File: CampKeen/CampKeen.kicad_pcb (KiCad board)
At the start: 4 copper layers, 177.8 x 142.2 mm, 181 parts, among them IC1 LM2597MX-ADJ_NOPB, IC2 LM2670SX-5.0_NOPB, IC3 DS3231SN#, IC4 CD74HC4050ME4, IC5 TL071CP, J1 Vin, J2 CircuitSetupsSplitPhase, J3 Vin, J4 Screw_Terminal_01x04, J5 GenEnclosure, J6 GenHeadL, J7 GenHeadR, K1 DIP05-1A72-12L, K2 DIP05-1A72-12L, K4 DIP05-1A72-12L, P1 Power, P10 CONN_01X01, P11 CONN_01X01, P12 CONN_01X01, P13 CONN_01X01, P2 Analog, P3 Analog, P4 Digital, P5 PWM, P6 PWM, P7 Communication, P8 CONN_01X01, P9 CONN_01X01, Q1 BC547, Q10 2N7000, Q11 2N7000, Q12 2N7000, Q13 2N7000, Q14 2N7000, Q15 IRF510, Q16 2N7000, Q17 IRF510, Q18 2N7000, Q19 IRF510, Q2 2N7000, Q20 2N7000, Q21 IRF510, Q22 BC547, Q23 2N7000, Q24 IRF510, Q25 2N7000, Q26 2N7000, Q27 IRF510, Q28 2N7000, Q29 IRF510, Q3 2N7000, Q30 2N7000, Q31 IRF510, Q32 BC547, Q33 2N7000, Q35 2N7000, Q36 IRF510, Q37 2N7000, Q38 IRF510, Q39 IRF510, Q4 2N7000, Q40 IRF9Z34NPBF, Q5 2N7000, Q6 BC547, Q7 2N7000, Q8 2N7000, Q9 2N7000, U2 MAX232

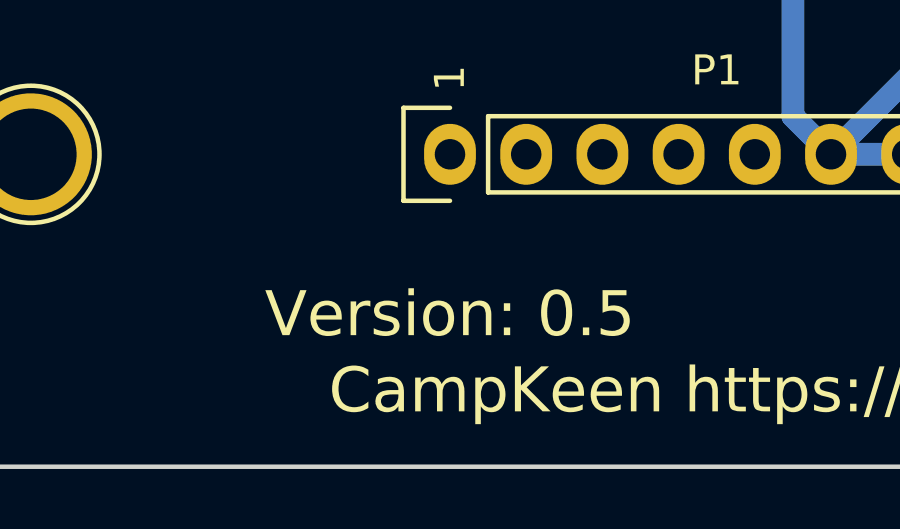
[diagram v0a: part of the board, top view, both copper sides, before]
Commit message: forgot to bump the version number to 0.6 on the PCB Silkscreen
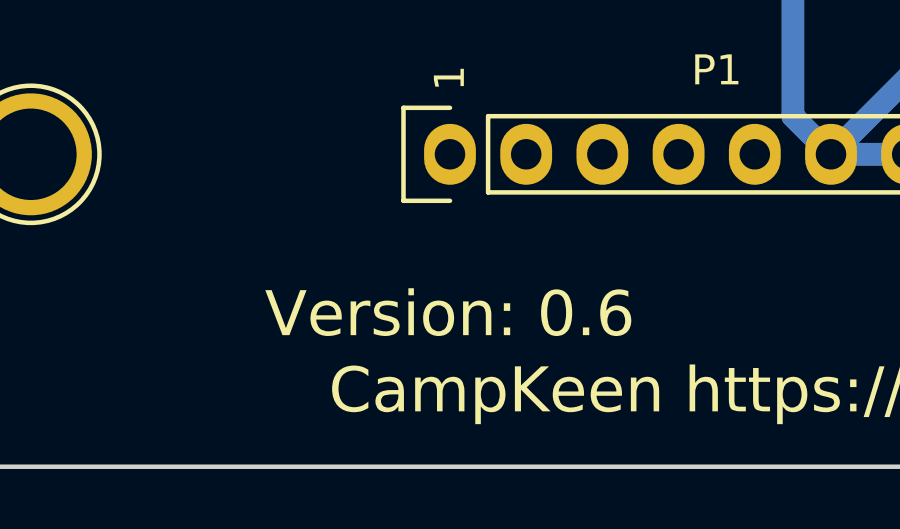
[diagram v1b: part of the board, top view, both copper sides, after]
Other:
- board text added: "Version: 0.6"
- board text removed: "Version: 0.5"

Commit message: adding docs and cleaning up pin mappings and extra parts for ports.
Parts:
- removed Q35: 2N7000, Package_TO_SOT_THT:TO-92_Inline
- removed R81, R83: 1M, Resistor_THT:R_Axial_DIN0207_L6.3mm_D2.5mm_P2.54mm_Vertical
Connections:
- IO1 pad 10: Net-(IO1-Pad10) -> (no net)
- Temps1 pad 4: +5V -> (no net)
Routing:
- net Net-(IO1-Pad10): track 131.6 -> 0.00 mm, vias 1 -> 0
- net Net-(Q35-Pad1): track 7.17 -> 0.00 mm
- net +5V: track 708.0 -> 701.8 mm

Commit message: continue on fixing and adding stuff. fixed the fuck up on the schematic for the 5to3 volt converter. changing out the voltage sensor to a opa2340, ading asecond general voltage sensor. and an additional NTC sensor. RTC Battery monitor.
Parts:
- added J8: Conn_01x02, Connector_PinHeader_2.54mm:PinHeader_1x02_P2.54mm_Vertical, F.Cu at (95.8, 6.35)
- added R25: 10k, Resistor_THT:R_Axial_DIN0207_L6.3mm_D2.5mm_P2.54mm_Vertical, F.Cu at (127.5, 165.1)
- added R29: 47K, Resistor_THT:R_Axial_DIN0207_L6.3mm_D2.5mm_P2.54mm_Vertical, F.Cu at (95.8, -6.35)
- added RV1: R_POT_US, Potentiometer_THT:Potentiometer_Bourns_3296W_Vertical, F.Cu at (90.4, 7.25)
- IC5: value TL071CP -> OPA2340PA
- moved IC5 28.0 mm to (88.1, -2.54)
- renumbered Tanks2 to Tanks0
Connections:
- net /A10 renamed A10
- net /A3 renamed A3
- net /A4 renamed A4
- net /A5 renamed A5
- net /A6 renamed A6
- net /A7 renamed A7
- net /A8 renamed A8
- net /A9 renamed A9
- net /CS renamed /3.3CS
- net /SCLK renamed /3.3SCLK
- IC3 pad 14: Net-(IC3-Pad14) -> A14
- IC4 pad 5: /50(MISO) -> /3.3MISO
- IC4 pad 6: /51(MOSI) -> /3.3MOSI
- IC5 pad 1: (no net) -> A0
- IC5 pad 2: /A0 -> A0
- IC5 pad 5: (no net) -> Net-(IC5-Pad5)
- IC5 pad 6: /A0 -> A12
- IC5 pad 7: +5V -> A12
- IC5 pad 8: (no net) -> +5V
- IO1 pad 10: (no net) -> AUXVoltage
- J2 pad 3: /51(MOSI) -> /3.3MOSI
- J2 pad 4: /50(MISO) -> /3.3MISO
- P2 pad 1: /A0 -> A0
- P3 pad 4: (no net) -> A11
- P3 pad 5: (no net) -> A12
- P3 pad 7: /A14 -> A14
- P3 pad 8: /A15 -> (no net)
- R35 pad 2: /A0 -> A0
- RTCBattery1 pad 1: Net-(IC3-Pad14) -> A14
- Tanks0 pad 11: /A14 -> (no net)
- Tanks0 pad 12: /A15 -> (no net)
- Temps1 pad 4: (no net) -> A11
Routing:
- net /50(MISO): track 251.5 -> 0.00 mm, vias 1 -> 0
- net /51(MOSI): track 251.4 -> 0.00 mm, vias 1 -> 0
- net /A0: track 150.9 -> 0.00 mm
- net /A15: track 137.5 -> 0.00 mm, vias 4 -> 0
- net /A14: track 131.4 -> 0.00 mm
- net Net-(IC3-Pad14): track 36.4 -> 0.00 mm, vias 2 -> 0
- net A14: track 0.00 -> 36.4 mm, vias 0 -> 2
- net GND: track 892.0 -> 875.8 mm
- net Net-(IC5-Pad3): track 20.3 -> 6.13 mm
- net +5V: track 701.8 -> 693.3 mm

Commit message: updated the pin mapping to the terms. cleaned up the Schematic. PCB placement and routing is what is left to do.
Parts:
- removed the IC5 at (88.1, -2.54)
- removed the J4 at (52.6, 95.2)
- removed K1, K2, K4: DIP05-1A72-12L, SamacSys_Parts:DIP051A7212L
- removed the Q1 at (182.1, 127.0)
- removed the R10 at (164.3, 128.8)
- removed the R7 at (182.6, 121.9)
- removed the R8 at (182.6, 116.8)
- removed the R9 at (159.3, 128.8)
- added 5VOut1: VS, SamacSys_Parts:BK_HTC-15M, F.Cu at (-49.0, -77.5)
- added C16: 22nF, Capacitor_THT:C_Disc_D4.7mm_W2.5mm_P5.00mm, F.Cu at (58.5, -26.7)
- added C17: 22nF, Capacitor_THT:C_Disc_D4.7mm_W2.5mm_P5.00mm, F.Cu at (71.9, -34.2)
- added C18: 22nF, Capacitor_THT:C_Disc_D4.7mm_W2.5mm_P5.00mm, F.Cu at (86.3, -38.1)
- added C19: 22nF, Capacitor_THT:C_Disc_D4.7mm_W2.5mm_P5.00mm, F.Cu at (58.5, -30.7)
- added C20: 22nF, Capacitor_THT:C_Disc_D4.7mm_W2.5mm_P5.00mm, F.Cu at (-97.3, -70.3)
- added C21: 22nF, Capacitor_THT:C_Disc_D4.7mm_W2.5mm_P5.00mm, F.Cu at (-110.7, -66.9)
- added C22: 22nF, Capacitor_THT:C_Disc_D4.7mm_W2.5mm_P5.00mm, F.Cu at (-82.9, -74.3)
- added C23: 22nF, Capacitor_THT:C_Disc_D4.7mm_W2.5mm_P5.00mm, F.Cu at (-110.7, -62.8)
- added C24: 22nF, Capacitor_THT:C_Disc_D4.7mm_W2.5mm_P5.00mm, F.Cu at (4.61, -12.7)
- added C25: 22nF, Capacitor_THT:C_Disc_D4.7mm_W2.5mm_P5.00mm, F.Cu at (4.61, -8.70)
- added C26: 22nF, Capacitor_THT:C_Disc_D4.7mm_W2.5mm_P5.00mm, F.Cu at (12.8, -12.7)
- added C27: 22nF, Capacitor_THT:C_Disc_D4.7mm_W2.5mm_P5.00mm, F.Cu at (4.61, -4.64)
- added C28: 22nF, Capacitor_THT:C_Disc_D4.7mm_W2.5mm_P5.00mm, F.Cu at (12.8, -36.3)
- added C29: 22nF, Capacitor_THT:C_Disc_D4.7mm_W2.5mm_P5.00mm, F.Cu at (20.9, -44.4)
- added C30: 22nF, Capacitor_THT:C_Disc_D4.7mm_W2.5mm_P5.00mm, F.Cu at (4.61, -32.2)
- added C31: 22nF, Capacitor_THT:C_Disc_D4.7mm_W2.5mm_P5.00mm, F.Cu at (12.8, -40.3)
- added C32: 22nF, Capacitor_THT:C_Disc_D4.7mm_W2.5mm_P5.00mm, F.Cu at (4.61, -36.3)
- added C33: 22nF, Capacitor_THT:C_Disc_D4.7mm_W2.5mm_P5.00mm, F.Cu at (12.8, -44.4)
- added C34: 22nF, Capacitor_THT:C_Disc_D4.7mm_W2.5mm_P5.00mm, F.Cu at (4.61, -40.3)
- added C35: 22nF, Capacitor_THT:C_Disc_D4.7mm_W2.5mm_P5.00mm, F.Cu at (4.61, -44.4)
- added C36: 22nF, Capacitor_THT:C_Disc_D4.7mm_W2.5mm_P5.00mm, F.Cu at (20.9, -40.3)
- added C37: 22nF, Capacitor_THT:C_Disc_D4.7mm_W2.5mm_P5.00mm, F.Cu at (4.61, -28.2)
- added IC4: OPA2340PA, SamacSys_Parts:DIP794W53P254L959H508Q8N, F.Cu at (-29.7, -76.7)
- added IC6: OPA2340PA, SamacSys_Parts:DIP794W53P254L959H508Q8N, F.Cu at (-57.5, -66.5)
- added J3: Conn_01x02, Connector_PinHeader_2.54mm:PinHeader_1x02_P2.54mm_Vertical, F.Cu at (-21.9, -73.0)
- added J9: Conn_01x02, Connector_PinHeader_2.54mm:PinHeader_1x02_P2.54mm_Vertical, F.Cu at (-21.9, -80.2)
- added Q34: IRF9Z34NPBF, SamacSys_Parts:TO254P469X1042X1967-3P, F.Cu at (32.0, -71.4)
- added Q35: 2N7000, Package_TO_SOT_THT:TO-92_Inline, F.Cu at (30.5, -65.9)
- added Q40: 2N7000, Package_TO_SOT_THT:TO-92_Inline, F.Cu at (50.4, -75.6)
- added Q41: IRF9Z34NPBF, SamacSys_Parts:TO254P469X1042X1967-3P, F.Cu at (6.54, -57.5)
- added Q42: IRF9Z34NPBF, SamacSys_Parts:TO254P469X1042X1967-3P, F.Cu at (33.3, -77.7)
- added Q43: 2N7000, Package_TO_SOT_THT:TO-92_Inline, F.Cu at (43.9, -75.6)
- added Q44: IRF9Z34NPBF, SamacSys_Parts:TO254P469X1042X1967-3P, F.Cu at (46.7, -81.1)
- added Q45: 2N7000, Package_TO_SOT_THT:TO-92_Inline, F.Cu at (5.02, -52.0)
- added Q46: IRF9Z34NPBF, SamacSys_Parts:TO254P469X1042X1967-3P, F.Cu at (19.9, -68.0)
- added Q47: 2N7000, Package_TO_SOT_THT:TO-92_Inline, F.Cu at (126.9, -11.9)
- added Q48: IRF9Z34NPBF, SamacSys_Parts:TO254P469X1042X1967-3P, F.Cu at (136.6, -20.9)
- added Q49: 2N7000, Package_TO_SOT_THT:TO-92_Inline, F.Cu at (133.8, -15.4)
- added Q50: IRF9Z34NPBF, SamacSys_Parts:TO254P469X1042X1967-3P, F.Cu at (109.8, -10.5)
- added Q51: 2N7000, Package_TO_SOT_THT:TO-92_Inline, F.Cu at (120.4, -11.2)
- added Q52: IRF9Z34NPBF, SamacSys_Parts:TO254P469X1042X1967-3P, F.Cu at (109.8, -4.28)
- added Q53: 2N7000, Package_TO_SOT_THT:TO-92_Inline, F.Cu at (120.4, -5.45)
- added Q54: IRF9Z34NPBF, SamacSys_Parts:TO254P469X1042X1967-3P, F.Cu at (123.2, -17.5)
- added Q55: IRF9Z34NPBF, SamacSys_Parts:TO254P469X1042X1967-3P, F.Cu at (-108.8, -46.0)
- added R100: 1M, Resistor_THT:R_Axial_DIN0207_L6.3mm_D2.5mm_P2.54mm_Vertical, F.Cu at (145.4, -6.79)
- added R101: 100k, Resistor_THT:R_Axial_DIN0207_L6.3mm_D2.5mm_P2.54mm_Vertical, F.Cu at (139.2, -2.75)
- added R102: 10k, Resistor_THT:R_Axial_DIN0207_L6.3mm_D2.5mm_P2.54mm_Vertical, F.Cu at (145.7, -12.6)
- added R103: 1M, Resistor_THT:R_Axial_DIN0207_L6.3mm_D2.5mm_P2.54mm_Vertical, F.Cu at (139.2, -6.79)
- added R104: 100k, Resistor_THT:R_Axial_DIN0207_L6.3mm_D2.5mm_P2.54mm_Vertical, F.Cu at (126.9, -7.38)
- added R105: 10k, Resistor_THT:R_Axial_DIN0207_L6.3mm_D2.5mm_P2.54mm_Vertical, F.Cu at (126.9, -3.33)
- added R106: 1M, Resistor_THT:R_Axial_DIN0207_L6.3mm_D2.5mm_P2.54mm_Vertical, F.Cu at (140.3, -16.6)
- added R107: 100k, Resistor_THT:R_Axial_DIN0207_L6.3mm_D2.5mm_P2.54mm_Vertical, F.Cu at (133.4, -10.8)
- added R108: 10k, Resistor_THT:R_Axial_DIN0207_L6.3mm_D2.5mm_P2.54mm_Vertical, F.Cu at (133.1, -6.79)
- added R109: 1M, Resistor_THT:R_Axial_DIN0207_L6.3mm_D2.5mm_P2.54mm_Vertical, F.Cu at (139.6, -10.8)
- added R110: 100k, Resistor_THT:R_Axial_DIN0207_L6.3mm_D2.5mm_P2.54mm_Vertical, F.Cu at (146.5, -16.6)
- added R111: 10k, Resistor_THT:R_Axial_DIN0207_L6.3mm_D2.5mm_P2.54mm_Vertical, F.Cu at (133.1, -2.75)
- added R112: 47K, Resistor_THT:R_Axial_DIN0207_L6.3mm_D2.5mm_P2.54mm_Vertical, F.Cu at (-32.7, -61.6)
- added R113: 47K, Resistor_THT:R_Axial_DIN0207_L6.3mm_D2.5mm_P2.54mm_Vertical, F.Cu at (-26.5, -61.6)
- added R114: 1M, Resistor_THT:R_Axial_DIN0207_L6.3mm_D2.5mm_P2.54mm_Vertical, F.Cu at (-110.3, -41.7)
- added R115: 100k, Resistor_THT:R_Axial_DIN0207_L6.3mm_D2.5mm_P2.54mm_Vertical, F.Cu at (-98.2, -45.7)
- added R116: 10k, Resistor_THT:R_Axial_DIN0207_L6.3mm_D2.5mm_P2.54mm_Vertical, F.Cu at (-104.1, -41.6)
- added R117: 330, Resistor_THT:R_Axial_DIN0207_L6.3mm_D2.5mm_P2.54mm_Vertical, F.Cu at (93.5, 13.0)
- added R28: 10k, Resistor_THT:R_Axial_DIN0207_L6.3mm_D2.5mm_P2.54mm_Vertical, F.Cu at (-60.9, -52.4)
- added R30: 10k, Resistor_THT:R_Axial_DIN0207_L6.3mm_D2.5mm_P2.54mm_Vertical, F.Cu at (-48.6, -48.3)
- added R35: 47, Resistor_THT:R_Axial_DIN0207_L6.3mm_D2.5mm_P2.54mm_Vertical, F.Cu at (65.1, -1.61)
- added R36: 47, Resistor_THT:R_Axial_DIN0207_L6.3mm_D2.5mm_P2.54mm_Vertical, F.Cu at (84.5, -5.08)
- added R81: 10k, Resistor_THT:R_Axial_DIN0207_L6.3mm_D2.5mm_P2.54mm_Vertical, F.Cu at (48.8, -54.9)
- added R82: 1M, Resistor_THT:R_Axial_DIN0207_L6.3mm_D2.5mm_P2.54mm_Vertical, F.Cu at (55.7, -61.1)
- added R83: 1M, Resistor_THT:R_Axial_DIN0207_L6.3mm_D2.5mm_P2.54mm_Vertical, F.Cu at (43.2, -63.0)
- added R89: 1M, Resistor_THT:R_Axial_DIN0207_L6.3mm_D2.5mm_P2.54mm_Vertical, F.Cu at (43.2, -67.0)
- added R90: 100k, Resistor_THT:R_Axial_DIN0207_L6.3mm_D2.5mm_P2.54mm_Vertical, F.Cu at (31.1, -58.9)
- added R91: 10k, Resistor_THT:R_Axial_DIN0207_L6.3mm_D2.5mm_P2.54mm_Vertical, F.Cu at (57.4, -77.3)
- added R92: 100k, Resistor_THT:R_Axial_DIN0207_L6.3mm_D2.5mm_P2.54mm_Vertical, F.Cu at (18.1, -51.6)
- added R93: 10k, Resistor_THT:R_Axial_DIN0207_L6.3mm_D2.5mm_P2.54mm_Vertical, F.Cu at (24.2, -51.6)
- added R94: 1M, Resistor_THT:R_Axial_DIN0207_L6.3mm_D2.5mm_P2.54mm_Vertical, F.Cu at (48.8, -71.1)
- added R95: 100k, Resistor_THT:R_Axial_DIN0207_L6.3mm_D2.5mm_P2.54mm_Vertical, F.Cu at (37.1, -67.0)
- added R96: 10k, Resistor_THT:R_Axial_DIN0207_L6.3mm_D2.5mm_P2.54mm_Vertical, F.Cu at (37.1, -63.0)
- added R97: 1M, Resistor_THT:R_Axial_DIN0207_L6.3mm_D2.5mm_P2.54mm_Vertical, F.Cu at (42.6, -71.1)
- added R98: 100k, Resistor_THT:R_Axial_DIN0207_L6.3mm_D2.5mm_P2.54mm_Vertical, F.Cu at (37.2, -58.9)
- added R99: 10k, Resistor_THT:R_Axial_DIN0207_L6.3mm_D2.5mm_P2.54mm_Vertical, F.Cu at (36.5, -54.9)
- added RV2: 500k, Potentiometer_THT:Potentiometer_Bourns_3296W_Vertical, F.Cu at (-32.7, -67.6)
- added RV3: 500k, Potentiometer_THT:Potentiometer_Bourns_3296W_Vertical, F.Cu at (-43.9, -62.7)
- added Tanks2: TanksVS, SamacSys_Parts:BK_HTC-15M, F.Cu at (-98.4, -77.5)
- added Z1: BZX79C10, SamacSys_Parts:DIOAD1068W53L380D172, F.Cu at (58.3, -34.5)
- added Z10: BZX79C10, SamacSys_Parts:DIOAD1068W53L380D172, F.Cu at (4.39, -79.9)
- added Z11: BZX79C10, SamacSys_Parts:DIOAD1068W53L380D172, F.Cu at (4.39, -83.4)
- added Z12: BZX79C10, SamacSys_Parts:DIOAD1068W53L380D172, F.Cu at (107.7, -19.7)
- added Z13: BZX79C10, SamacSys_Parts:DIOAD1068W53L380D172, F.Cu at (121.1, -23.2)
- added Z14: BZX79C10, SamacSys_Parts:DIOAD1068W53L380D172, F.Cu at (107.7, -16.2)
- added Z15: BZX79C10, SamacSys_Parts:DIOAD1068W53L380D172, F.Cu at (107.7, -23.2)
- added Z16: BZX79C10, SamacSys_Parts:DIOAD1068W53L380D172, F.Cu at (-110.9, -51.7)
- added Z2: BZX79C10, SamacSys_Parts:DIOAD1068W53L380D172, F.Cu at (58.3, -5.38)
- added Z3: BZX79C10, SamacSys_Parts:DIOAD1068W53L380D172, F.Cu at (-110.9, -70.6)
- added Z4: BZX79C10, SamacSys_Parts:DIOAD1068W53L380D172, F.Cu at (4.39, -69.5)
- added Z5: BZX79C10, SamacSys_Parts:DIOAD1068W53L380D172, F.Cu at (4.39, -73.0)
- added Z6: BZX79C10, SamacSys_Parts:DIOAD1068W53L380D172, F.Cu at (17.8, -79.9)
- added Z7: BZX79C10, SamacSys_Parts:DIOAD1068W53L380D172, F.Cu at (31.2, -83.4)
- added Z8: BZX79C10, SamacSys_Parts:DIOAD1068W53L380D172, F.Cu at (4.39, -76.4)
- added Z9: BZX79C10, SamacSys_Parts:DIOAD1068W53L380D172, F.Cu at (17.8, -83.4)
- IO1: renamed from Tanks0; value Tanks -> IO1
- IO2: renamed from I1; value I1 -> IO2
- IO3: renamed from O1; value O1 -> IO3
- IO4: renamed from IO1; value IO2 -> IO4
- Q10, Q12, Q33, Q37, Q4: value 2N7000 -> IRF9Z34NPBF; footprint Package_TO_SOT_THT:TO-92_Inline -> SamacSys_Parts:TO254P469X1042X1967-3P
- Q15, Q17, Q19, Q21, Q24, Q27, Q29, Q31, Q36, Q39: value IRF510 -> 2N7000; footprint SamacSys_Parts:TO254P465X1024X2050-3P -> Package_TO_SOT_THT:TO-92_Inline
- Q22, Q32, Q6: value BC547 -> 2N7000
- Q38: value IRF510 -> IRF9Z34NPBF; footprint SamacSys_Parts:TO254P465X1024X2050-3P -> SamacSys_Parts:TO254P469X1042X1967-3P
- R11: value 1M -> 47K
- R13, R33, R38, R80, R84, R86: value 1M -> 100k
- R14, R31, R34, R39, R79, R85, R87: value 1M -> 10k
- R16, R17, R19, R20, R21, R22, R58, R76: value 10k -> 1M
- R27: value 100k -> 10k
- R29: value 47K -> 10k
- R61: value 100k -> 1M
- R70, R74: value 47 -> 1M
- RV1: value R_POT_US -> 500k
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- renumbered C7 to C10, C5 to C11, C14 to C12, C15 to C13, C16 to C14, C17 to C15, C9 to C3, C18 to C4, C3 to C5, C8 to C6, C4 to C7, C6 to C8, C10 to C9, IC4 to IC5, J3 to J2, J2 to J4, L2 to L1, L1 to L2, Q40 to Q1, R6 to R10, R89 to R5, R28 to R6, R82 to R7, R35 to R8, R5 to R9, U2 to U1
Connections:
- net /16(Tx2) renamed COMTXTTL
- net /17(Rx2) renamed COMRXTTL
- net /45 renamed GenHR-CS
- net /47 renamed GenHL-CS
- net /49 renamed GenE-CS
- net /50(MISO) renamed MISO
- net /51(MOSI) renamed MOSI
- net /52(SCK) renamed CLK
- IC3 pad 15: /20(SDA) -> SDA
- IC3 pad 16: /21(SCL) -> SCL
- IC5 pad 14: /41 -> EnCS
- IO1 pad 1: Net-(Q2-Pad2) -> A2
- IO1 pad 10: Net-(K2-Pad1) -> IO110
- IO1 pad 11: (no net) -> IO111
- IO1 pad 12: (no net) -> IO112
- IO1 pad 2: Net-(Q3-Pad2) -> IO12
- IO1 pad 3: Net-(Q4-Pad2) -> IO13
- IO1 pad 4: Net-(Q5-Pad2) -> IO14
- IO1 pad 5: Net-(Q7-Pad2) -> IO15
- IO1 pad 6: Net-(Q8-Pad2) -> IO16
- IO1 pad 7: Net-(Q9-Pad2) -> IO17
- IO1 pad 8: Net-(Q10-Pad2) -> IO18
- IO1 pad 9: Net-(K1-Pad1) -> IO19
- IO2 pad 1: Net-(I1-Pad1) -> Net-(5VOut1-Pad2)
- IO2 pad 10: Net-(I1-Pad10) -> A1
- IO2 pad 11: Net-(I1-Pad11) -> IO211
- IO2 pad 12: Net-(I1-Pad12) -> IO212
- IO2 pad 2: Net-(I1-Pad2) -> IO22
- IO2 pad 3: Net-(I1-Pad3) -> IO23
- IO2 pad 4: Net-(I1-Pad4) -> IO24
- IO2 pad 5: Net-(I1-Pad5) -> IO25
- IO2 pad 6: Net-(I1-Pad6) -> IO26
- IO2 pad 7: Net-(I1-Pad7) -> IO27
- IO2 pad 8: Net-(I1-Pad8) -> IO28
- IO2 pad 9: Net-(I1-Pad9) -> IO29
- IO3 pad 1: Net-(O1-Pad1) -> IO31
- IO3 pad 10: Net-(O1-Pad10) -> RX232
- IO3 pad 11: Net-(O1-Pad11) -> IO311
- IO3 pad 12: Net-(O1-Pad12) -> AUXVoltage2
- IO3 pad 2: Net-(O1-Pad2) -> IO32
- IO3 pad 3: Net-(O1-Pad3) -> IO33
- IO3 pad 4: Net-(O1-Pad4) -> IO34
- IO3 pad 5: Net-(O1-Pad5) -> IO35
- IO3 pad 6: Net-(O1-Pad6) -> AUXVoltage
- IO3 pad 7: Net-(O1-Pad7) -> TX232
- IO3 pad 8: Net-(O1-Pad8) -> IO38
- IO3 pad 9: Net-(O1-Pad9) -> AUXVoltage1
- IO4 pad 1: Net-(IO1-Pad1) -> IO41
- IO4 pad 10: AUXVoltage -> IO410
- IO4 pad 11: /A13 -> IO411
- IO4 pad 12: /A2 -> IO412
- IO4 pad 2: Net-(IO1-Pad2) -> IO42
- IO4 pad 3: Net-(IO1-Pad3) -> SDA
- IO4 pad 4: Net-(IO1-Pad4) -> IO44
- IO4 pad 5: Net-(IO1-Pad5) -> IO45
- IO4 pad 6: /A1 -> SCL
- IO4 pad 7: +9V -> IO47
- IO4 pad 8: Net-(IO1-Pad8) -> IO48
- IO4 pad 9: Net-(IO1-Pad9) -> IO49
- LPWater1 pad 1: Net-(K4-Pad7) -> Net-(LPWater1-Pad1)
- P2 pad 2: /A1 -> A1
- P2 pad 3: /A2 -> A2
- P3 pad 6: /A13 -> A13
- P3 pad 8: (no net) -> A15
- P4 pad 11: /44 -> S3-4
- P4 pad 13: /42 -> S4-4
- P4 pad 14: /43 -> WPS
- P4 pad 15: /40 -> G1-4
- P4 pad 16: /41 -> ENLCD
- P4 pad 17: /38 -> G1-2
- P4 pad 18: /39 -> LCBBACK
- P4 pad 19: /36 -> G3-4
- P4 pad 20: /37 -> WSS
- P4 pad 21: /34 -> G4-4
- P4 pad 22: /35 -> SPIn1
- P4 pad 23: /32 -> GreyV
- P4 pad 24: /33 -> SPIn2
- P4 pad 25: /30 -> STV
- P4 pad 26: /31 -> SPIn3
- P4 pad 27: /28 -> CWV
- P4 pad 28: /29 -> SPIn4
- P4 pad 29: /26 -> WP
- P4 pad 30: /27 -> SPIn5
- P4 pad 31: /24 -> EnCS
- P4 pad 32: /25 -> SPIn6
- P4 pad 33: /D22 -> RTankPOWER
- P4 pad 34: /23 -> LCDPOWER
- P4 pad 7: /48 -> S1-4
- P4 pad 9: /46 -> S1-2
- P5 pad 1: /21(SCL) -> SCL
- P5 pad 10: /8(**) -> LCDBL
- P5 pad 2: /20(SDA) -> SDA
- P5 pad 6: /12(**) -> SO1
- P5 pad 7: /11(**) -> SO2
- P5 pad 8: /10(**) -> SO3
- P5 pad 9: /9(**) -> SO4
- P6 pad 1: /7(**) -> BRLED
- P6 pad 2: /6(**) -> KLED
- P6 pad 3: /5(**) -> WLED
- P6 pad 4: /4(**) -> WSiren
- P6 pad 5: /3(**) -> AlarmTTL
- P6 pad 6: /2(**) -> SpareTTL
- P7 pad 1: /14(Tx3) -> SO5
- P7 pad 2: /15(Rx3) -> (no net)
- P7 pad 5: /18(Tx1) -> KitchenTTL
- P7 pad 6: /19(Rx1) -> BathRoomTTL
- P7 pad 7: /20(SDA) -> SDA
- P7 pad 8: /21(SCL) -> SCL
- Q10 pad 1: /34 -> Net-(Q10-Pad1)
- Q10 pad 2: Net-(Q10-Pad2) -> IO14
- Q10 pad 3: +5V -> Net-(LPWater1-Pad1)
- Q11 pad 1: /23 -> GND
- Q11 pad 2: Net-(I1-Pad1) -> GreyV
- Q11 pad 3: +5V -> Net-(Q11-Pad3)
- Q12 pad 1: /2(**) -> Net-(Q12-Pad1)
- Q12 pad 2: Net-(I1-Pad2) -> IO110
- Q12 pad 3: +5V -> Net-(Q12-Pad3)
- Q13 pad 1: /3(**) -> G1-4
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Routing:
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- removed copper zone on F.Cu, net GND
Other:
- board text added: "Version: 1.0 ALPHA"
- board text removed: "Gen Head L"
- board text removed: "Holding Tank Sensors"
- board text removed: "OUTPUTS"
- board text removed: "RS232"
- board text removed: "SDA SCL GND 5V"
- board text removed: "Version: 0.6"

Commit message: fixed the Diode orientation.
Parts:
- added D3: LED, LED_THT:LED_D3.0mm, F.Cu at (-54.1, 14.0)
- moved R117 181.2 mm to (-85.9, -12.7)
- moved R6 178.8 mm to (-78.2, -16.5)
- moved R7 178.8 mm to (-78.2, -11.4)
- moved R8 178.8 mm to (-78.2, -6.35)
- moved J5 7.62 mm to (203.2, 76.2)
- moved J7 7.62 mm to (202.9, 103.9)
- moved J6 7.62 mm to (202.6, 132.1)
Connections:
- P5 pad 5: (no net) -> DisplayLED
- R117 pad 2: (no net) -> Net-(D3-Pad1)
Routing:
- net +12V: track 99.8 -> 50.4 mm
- net Net-(Main1-Pad2): track 21.5 -> 0.00 mm
- net Net-(Q1-Pad1): track 3.81 -> 0.00 mm
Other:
- board text added: "Gen Head L"
- board text removed: "Voltage Sensor"

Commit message: separated the 12 and 5 volt outputs. added another spare output.
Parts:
- removed the Q31 at (57.3, -81.9)
- removed the Q33 at (18.6, -61.7)
- removed the Q35 at (30.5, -65.9)
- removed the Q37 at (6.54, -63.8)
- removed the Q40 at (50.4, -75.6)
- removed the Q42 at (33.3, -77.7)
- removed the R76 at (55.5, -69.2)
- removed the R78 at (49.5, -58.9)
- removed the R84 at (49.3, -63.0)
- removed the R85 at (43.4, -58.9)
- removed the R89 at (43.2, -67.0)
- removed the R92 at (18.1, -51.6)
- removed the R93 at (24.2, -51.6)
- removed the Z6 at (17.8, -79.9)
- removed the Z9 at (17.8, -83.4)
- added Q30: 2N7000, Package_TO_SOT_THT:TO-92_Inline, F.Cu at (210.3, -63.7)
- added Q32: IRF9Z34NPBF, SamacSys_Parts:TO254P469X1042X1967-3P, F.Cu at (198.4, -59.5)
- added Q43: 2N7000, Package_TO_SOT_THT:TO-92_Inline, F.Cu at (210.3, -46.8)
- added Q45: IRF9Z34NPBF, SamacSys_Parts:TO254P469X1042X1967-3P, F.Cu at (198.4, -42.7)
- added Q54: 2N7000, Package_TO_SOT_THT:TO-92_Inline, F.Cu at (158.9, -50.5)
- added Q55: IRF9Z34NPBF, SamacSys_Parts:TO254P469X1042X1967-3P, F.Cu at (173.9, -63.0)
- added Q56: 2N7000, Package_TO_SOT_THT:TO-92_Inline, F.Cu at (172.3, -57.5)
- added Q57: IRF9Z34NPBF, SamacSys_Parts:TO254P469X1042X1967-3P, F.Cu at (160.5, -56.1)
- added R101: 100k, Resistor_THT:R_Axial_DIN0207_L6.3mm_D2.5mm_P2.54mm_Vertical, F.Cu at (209.0, -42.3)
- added R102: 10k, Resistor_THT:R_Axial_DIN0207_L6.3mm_D2.5mm_P2.54mm_Vertical, F.Cu at (196.9, -38.4)
- added R115: 1M, Resistor_THT:R_Axial_DIN0207_L6.3mm_D2.5mm_P2.54mm_Vertical, F.Cu at (177.2, -50.6)
- added R116: 100k, Resistor_THT:R_Axial_DIN0207_L6.3mm_D2.5mm_P2.54mm_Vertical, F.Cu at (185.0, -60.9)
- added R117: 10k, Resistor_THT:R_Axial_DIN0207_L6.3mm_D2.5mm_P2.54mm_Vertical, F.Cu at (178.9, -54.7)
- added R118: 1M, Resistor_THT:R_Axial_DIN0207_L6.3mm_D2.5mm_P2.54mm_Vertical, F.Cu at (178.9, -58.7)
- added R119: 100k, Resistor_THT:R_Axial_DIN0207_L6.3mm_D2.5mm_P2.54mm_Vertical, F.Cu at (171.1, -52.9)
- added R120: 10k, Resistor_THT:R_Axial_DIN0207_L6.3mm_D2.5mm_P2.54mm_Vertical, F.Cu at (184.5, -65.0)
- added R81: 100k, Resistor_THT:R_Axial_DIN0207_L6.3mm_D2.5mm_P2.54mm_Vertical, F.Cu at (209.0, -59.2)
- added R98: 1M, Resistor_THT:R_Axial_DIN0207_L6.3mm_D2.5mm_P2.54mm_Vertical, F.Cu at (203.0, -38.2)
- added Z11: BZX79C10, SamacSys_Parts:DIOAD1068W53L380D172, F.Cu at (196.2, -48.4)
- added Z16: BZX79C10, SamacSys_Parts:DIOAD1068W53L380D172, F.Cu at (158.3, -61.8)
- added Z17: BZX79C10, SamacSys_Parts:DIOAD1068W53L380D172, F.Cu at (158.3, -65.2)
- J2: value Vin -> Screw_Terminal_01x03; footprint TerminalBlock_Phoenix:TerminalBlock_Phoenix_MKDS-1,5-2-5.08_1x02_P5.08mm_Horizontal -> TerminalBlock_Phoenix:TerminalBlock_Phoenix_MKDS-1,5-3-5.08_1x03_P5.08mm_Horizontal
- R79: value 10k -> 1M
- R82: value 1M -> 10k
- moved Z4 191.9 mm to (196.2, -65.2)
- moved R79 147.9 mm to (203.0, -55.1)
- moved R82 141.4 mm to (196.9, -55.2)
- moved J2 3.81 mm to (112.3, 24.1)
- moved Main1 1.27 mm to (119.9, 33.0)
- renumbered C9 to C10, C10 to C11, C11 to C3, C3 to C4, C4 to C5, C5 to C6, C6 to C7, C7 to C8, C8 to C9, IC5 to IC1, IC1 to IC2, IC2 to IC3, IC3 to IC4, IC4 to IC5, J4 to J3, J8 to J4, J3 to J5, J9 to J6, J5 to J7, J6 to J8, J7 to J9, Q11 to Q10, Q12 to Q11, Q13 to Q12, Q14 to Q13, Q15 to Q14, Q16 to Q15, Q17 to Q16, Q18 to Q17, Q19 to Q18, Q20 to Q19, Q3 to Q2, Q21 to Q20, Q22 to Q21, Q23 to Q22, Q24 to Q23, Q25 to Q24, Q26 to Q25, Q27 to Q26, Q28 to Q27, Q29 to Q28, Q30 to Q29, Q4 to Q3, Q32 to Q31, Q34 to Q33, Q36 to Q34, Q38 to Q35, Q39 to Q36, Q41 to Q37, Q43 to Q38, Q44 to Q39, Q5 to Q4, Q45 to Q40, Q46 to Q41, Q47 to Q42, Q48 to Q44, Q49 to Q46, Q50 to Q47, Q51 to Q48, Q52 to Q49, Q6 to Q5, Q53 to Q50, Q54 to Q51, Q2 to Q52, Q55 to Q53, Q7 to Q6, Q8 to Q7, Q9 to Q8, Q10 to Q9, R8 to R10, R102 to R100, R112 to R11, R114 to R112, R115 to R113, R116 to R114, R11 to R12, R113 to R13, R117 to R14, R12 to R15, R13 to R16, R14 to R17, R15 to R18, R16 to R19, R17 to R20, R18 to R21, R19 to R22, R20 to R23, R21 to R24, R22 to R25, R23 to R26, R24 to R27, R25 to R28, R26 to R29, R27 to R30, R28 to R31, R29 to R32, R30 to R33, R31 to R34, R32 to R35, R33 to R36, R34 to R37, R35 to R38, R36 to R39, R37 to R40, R38 to R41, R39 to R42, R40 to R43, R41 to R44, R42 to R45, R43 to R46, R44 to R47, R45 to R48, R46 to R49, R47 to R50, R48 to R51, R49 to R52, R50 to R53, R51 to R54, R52 to R55, R53 to R56, R54 to R57, R55 to R58, R56 to R59, R9 to R6, R57 to R60, R58 to R61, R59 to R62, R60 to R63, R61 to R64, R62 to R65, R63 to R66, R64 to R67, R65 to R68, R66 to R69, R10 to R7, R67 to R70, R68 to R71, R69 to R72, R70 to R73, R71 to R74, R72 to R75, R73 to R76, R74 to R77, R75 to R78, R6 to R8, R77 to R80, R80 to R83, R81 to R84, R83 to R85, R90 to R89, R7 to R9, R91 to R90, R94 to R91, R95 to R92, R96 to R93, R97 to R94, R98 to R95, R99 to R96, R100 to R97, R101 to R99, RV2 to RV1, RV1 to RV2, Z12 to Z10, Z13 to Z12, Z14 to Z13, Z15 to Z14, Z16 to Z15, Z7 to Z6, Z8 to Z7, Z10 to Z8, Z11 to Z9
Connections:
- P7 pad 2: (no net) -> SO6
- R79 pad 1: Net-(Q33-Pad1) (its old number) -> WSiren
- R79 pad 2: Net-(Q31-Pad3) (its old number) -> GND
- R82 pad 1: LCDBL -> Net-(Q32-Pad1)
- R82 pad 2: GND -> Net-(Q30-Pad3)
- Z4 pad 2: Net-(Q33-Pad1) (its old number) -> Net-(Q32-Pad1)

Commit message: cause i messed up a PR pretty badly with Github.
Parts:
- removed 5VOut1: VS, SamacSys_Parts:BK_HTC-15M
- removed the C16 at (58.5, -26.7)
- removed the C17 at (71.9, -34.2)
- removed the C18 at (86.3, -38.1)
- removed C19, C20, C21, C22, C23, C24, C25, C26, C27, C28, C29, C30, C31, C32, C33, C34, C35, C36, C37: 22nF, Capacitor_THT:C_Disc_D4.7mm_W2.5mm_P5.00mm
- removed D3: LED, LED_THT:LED_D3.0mm
- removed IC6: OPA2340PA, SamacSys_Parts:DIP794W53P254L959H508Q8N
- removed the J2 at (112.3, 24.1)
- removed the J5 at (-21.9, -73.0)
- removed the J6 at (-21.9, -80.2)
- removed Q34, Q42, Q43, Q46, Q48, Q50, Q52, Q54, Q56: 2N7000, Package_TO_SOT_THT:TO-92_Inline
- removed Q35, Q41, Q44, Q45, Q47, Q49, Q51, Q53, Q55, Q57: IRF9Z34NPBF, SamacSys_Parts:TO254P469X1042X1967-3P
- removed the Q40 at (5.02, -52.0)
- removed R100, R102, R105, R108, R111, R114, R117, R120, R29, R30, R90, R93, R96: 10k, Resistor_THT:R_Axial_DIN0207_L6.3mm_D2.5mm_P2.54mm_Vertical
- removed R101, R104, R107, R110, R113, R116, R119, R36, R81, R83, R92, R95, R99: 100k, Resistor_THT:R_Axial_DIN0207_L6.3mm_D2.5mm_P2.54mm_Vertical
- removed R103, R106, R109, R112, R115, R118, R25, R91, R94, R97, R98: 1M, Resistor_THT:R_Axial_DIN0207_L6.3mm_D2.5mm_P2.54mm_Vertical
- removed the R28 at (-60.9, -44.3)
- removed the R35 at (84.5, -1.03)
- removed the R82 at (196.9, -55.2)
- removed the R89 at (31.1, -58.9)
- removed RV1, RV2, RV3: 500k, Potentiometer_THT:Potentiometer_Bourns_3296W_Vertical
- removed the Tanks2 at (-98.4, -77.5)
- removed Z1, Z10, Z11, Z12, Z13, Z14, Z15, Z16, Z17, Z2, Z3, Z4, Z5, Z6, Z7, Z8, Z9: BZX79C10, SamacSys_Parts:DIOAD1068W53L380D172
- added J3: Vin, TerminalBlock_Phoenix:TerminalBlock_Phoenix_MKDS-1,5-2-5.08_1x02_P5.08mm_Horizontal, F.Cu at (108.5, 24.1)
- added K1: DIP05-1A72-12L, SamacSys_Parts:DIP051A7212L, F.Cu at (189.0, 111.8)
- added K2: DIP05-1A72-12L, SamacSys_Parts:DIP051A7212L, F.Cu at (202.4, 111.8)
- added K4: DIP05-1A72-12L, SamacSys_Parts:DIP051A7212L, F.Cu at (150.4, 63.5)
- added Q1: BC547, Package_TO_SOT_THT:TO-92_Inline, F.Cu at (182.1, 127.0)
- added R10: 1M, Resistor_THT:R_Axial_DIN0207_L6.3mm_D2.5mm_P2.54mm_Vertical, F.Cu at (164.3, 128.8)
- added R7: 10k, Resistor_THT:R_Axial_DIN0207_L6.3mm_D2.5mm_P2.54mm_Vertical, F.Cu at (182.6, 121.9)
- added R8: 100k, Resistor_THT:R_Axial_DIN0207_L6.3mm_D2.5mm_P2.54mm_Vertical, F.Cu at (182.6, 116.8)
- added R9: 1M, Resistor_THT:R_Axial_DIN0207_L6.3mm_D2.5mm_P2.54mm_Vertical, F.Cu at (159.3, 128.8)
- I1: renamed from IO2; value IO2 -> I1
- IC5: value OPA2340PA -> TL071CP
- IO1: renamed from IO4; value IO4 -> IO2
- J4: value Conn_01x02 -> Screw_Terminal_01x04; footprint Connector_PinHeader_2.54mm:PinHeader_1x02_P2.54mm_Vertical -> TerminalBlock_TE-Connectivity:TerminalBlock_TE_282834-4_1x04_P2.54mm_Horizontal
- O1: renamed from IO3; value IO3 -> O1
- Q11, Q3, Q33, Q37, Q9: value IRF9Z34NPBF -> 2N7000; footprint SamacSys_Parts:TO254P469X1042X1967-3P -> Package_TO_SOT_THT:TO-92_Inline
- Q15, Q17, Q19, Q21, Q24, Q27, Q29, Q31, Q36, Q38: value 2N7000 -> IRF510; footprint Package_TO_SOT_THT:TO-92_Inline -> SamacSys_Parts:TO254P465X1024X2050-3P
- Q22, Q6: value 2N7000 -> BC547
- Q32: value IRF9Z34NPBF -> BC547; footprint SamacSys_Parts:TO254P469X1042X1967-3P -> Package_TO_SOT_THT:TO-92_Inline
- Q39: value IRF9Z34NPBF -> IRF510; footprint SamacSys_Parts:TO254P469X1042X1967-3P -> SamacSys_Parts:TO254P465X1024X2050-3P
- R11, R12, R13: value 47K -> 1M
- R14: value 330 -> 1M
- R16: value 100k -> 10k
- R19, R20, R21, R22, R23, R24, R58, R76: value 1M -> 10k
- R27: value 10k -> 100k
- R31, R32, R33, R34, R37, R42, R84, R87: value 10k -> 1M
- R38, R39: value 47 -> 1M
- R41, R86: value 100k -> 1M
- R61, R78: value 1M -> 100k
- R70, R74: value 1M -> 47
- Tanks2: renamed from IO1; value IO1 -> Tanks
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- renumbered C12 to C14, C13 to C15, C14 to C16, C15 to C17, C5 to C18, C6 to C3, C8 to C4, C3 to C5, C9 to C6, C11 to C7, C7 to C8, C4 to C9, IC2 to IC1, IC3 to IC2, IC4 to IC3, IC1 to IC4, J3 to J2, J7 to J5, J8 to J6, J9 to J7, L2 to L1, L1 to L2, Q1 to Q40, R8 to R28, R10 to R35, R6 to R5, R7 to R6, R9 to R82, R5 to R89, U1 to U2
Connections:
- net /3.3CS renamed /CS
- net /3.3SCLK renamed /SCLK
- net CLK renamed /52(SCK)
- net COMRXTTL renamed /17(Rx2)
- net COMTXTTL renamed /16(Tx2)
- net GenE-CS renamed /49
- net GenHL-CS renamed /47
- net GenHR-CS renamed /45
- I1 pad 1: Net-(5VOut1-Pad2) -> Net-(I1-Pad1)
- I1 pad 10: A1 -> Net-(I1-Pad10)
- I1 pad 11: IO211 -> Net-(I1-Pad11)
- I1 pad 12: IO212 -> Net-(I1-Pad12)
- I1 pad 2: IO22 -> Net-(I1-Pad2)
- I1 pad 3: IO23 -> Net-(I1-Pad3)
- I1 pad 4: IO24 -> Net-(I1-Pad4)
- I1 pad 5: IO25 -> Net-(I1-Pad5)
- I1 pad 6: IO26 -> Net-(I1-Pad6)
- I1 pad 7: IO27 -> Net-(I1-Pad7)
- I1 pad 8: IO28 -> Net-(I1-Pad8)
- I1 pad 9: IO29 -> Net-(I1-Pad9)
- IC3 pad 14: A14 -> Net-(IC3-Pad14)
- IC3 pad 15: SDA -> /20(SDA)
- IC3 pad 16: SCL -> /21(SCL)
- IC4 pad 14: EnCS -> /41
- IC4 pad 4: MISO -> /50(MISO)
- IC4 pad 5: /3.3MISO -> /50(MISO)
- IC4 pad 6: /3.3MOSI -> /51(MOSI)
- IC4 pad 7: MOSI -> /51(MOSI)
- IC5 pad 1: A0 -> (no net)
- IC5 pad 2: A0 -> /A0
- IC5 pad 5: Net-(IC5-Pad5) -> (no net)
- IC5 pad 6: A12 -> /A0
- IC5 pad 7: A12 -> +5V
- IC5 pad 8: +5V -> (no net)
- IO1 pad 1: IO41 -> Net-(IO1-Pad1)
- IO1 pad 10: IO410 -> (no net)
- IO1 pad 11: IO411 -> /A13
- IO1 pad 12: IO412 -> /A2
- IO1 pad 2: IO42 -> Net-(IO1-Pad2)
- IO1 pad 3: SDA -> Net-(IO1-Pad3)
- IO1 pad 4: IO44 -> Net-(IO1-Pad4)
- IO1 pad 5: IO45 -> Net-(IO1-Pad5)
- IO1 pad 6: SCL -> /A1
- IO1 pad 7: IO47 -> +9V
- IO1 pad 8: IO48 -> Net-(IO1-Pad8)
- IO1 pad 9: IO49 -> Net-(IO1-Pad9)
- J2 pad 3: /3.3MOSI -> /51(MOSI)
- J2 pad 4: /3.3MISO -> /50(MISO)
- J4 pad 1: Net-(IC6-Pad3) -> /20(SDA)
- J4 pad 2: Net-(J4-Pad2) -> /21(SCL)
- J5 pad 5: MISO -> /50(MISO)
- J5 pad 6: MOSI -> /51(MOSI)
- J6 pad 5: MISO -> /50(MISO)
- J6 pad 6: MOSI -> /51(MOSI)
- J7 pad 5: MISO -> /50(MISO)
- J7 pad 6: MOSI -> /51(MOSI)
- LPWater1 pad 1: Net-(LPWater1-Pad1) -> Net-(K4-Pad7)
- O1 pad 1: IO31 -> Net-(O1-Pad1)
- O1 pad 10: RX232 -> Net-(O1-Pad10)
- O1 pad 11: IO311 -> Net-(O1-Pad11)
- O1 pad 12: AUXVoltage2 -> Net-(O1-Pad12)
- O1 pad 2: IO32 -> Net-(O1-Pad2)
- O1 pad 3: IO33 -> Net-(O1-Pad3)
- O1 pad 4: IO34 -> Net-(O1-Pad4)
- O1 pad 5: IO35 -> Net-(O1-Pad5)
- O1 pad 6: AUXVoltage -> Net-(O1-Pad6)
- O1 pad 7: TX232 -> Net-(O1-Pad7)
- O1 pad 8: IO38 -> Net-(O1-Pad8)
- O1 pad 9: AUXVoltage1 -> Net-(O1-Pad9)
- P2 pad 1: A0 -> /A0
- P2 pad 2: A1 -> /A1
- P2 pad 3: A2 -> /A2
- P2 pad 4: A3 -> /A3
- P2 pad 5: A4 -> /A4
- P2 pad 6: A5 -> /A5
- P2 pad 7: A6 -> /A6
- P2 pad 8: A7 -> /A7
- P3 pad 1: A8 -> /A8
- P3 pad 2: A9 -> /A9
- P3 pad 3: A10 -> /A10
- P3 pad 4: A11 -> (no net)
- P3 pad 5: A12 -> (no net)
- P3 pad 6: A13 -> /A13
- P3 pad 7: A14 -> /A14
- P3 pad 8: A15 -> /A15
- P4 pad 11: S3-4 -> /44
- P4 pad 13: S4-4 -> /42
- P4 pad 14: WPS -> /43
- P4 pad 15: G1-4 -> /40
- P4 pad 16: ENLCD -> /41
- P4 pad 17: G1-2 -> /38
- P4 pad 18: LCBBACK -> /39
- P4 pad 19: G3-4 -> /36
- P4 pad 20: WSS -> /37
- P4 pad 21: G4-4 -> /34
- P4 pad 22: SPIn1 -> /35
- P4 pad 23: GreyV -> /32
- P4 pad 24: SPIn2 -> /33
- P4 pad 25: STV -> /30
- P4 pad 26: SPIn3 -> /31
- P4 pad 27: CWV -> /28
- P4 pad 28: SPIn4 -> /29
- P4 pad 29: WP -> /26
- P4 pad 30: SPIn5 -> /27
- P4 pad 31: EnCS -> /24
- P4 pad 32: SPIn6 -> /25
- P4 pad 33: RTankPOWER -> /D22
- P4 pad 34: LCDPOWER -> /23
- P4 pad 5: MISO -> /50(MISO)
- P4 pad 6: MOSI -> /51(MOSI)
- P4 pad 7: S1-4 -> /48
- P4 pad 9: S1-2 -> /46
- P5 pad 1: SCL -> /21(SCL)
- P5 pad 10: LCDBL -> /8(**)
- P5 pad 2: SDA -> /20(SDA)
- P5 pad 5: DisplayLED -> (no net)
- P5 pad 6: SO1 -> /12(**)
- P5 pad 7: SO2 -> /11(**)
- P5 pad 8: SO3 -> /10(**)
- P5 pad 9: SO4 -> /9(**)
- P6 pad 1: BRLED -> /7(**)
- P6 pad 2: KLED -> /6(**)
- P6 pad 3: WLED -> /5(**)
- P6 pad 4: WSiren -> /4(**)
- P6 pad 5: AlarmTTL -> /3(**)
- P6 pad 6: SpareTTL -> /2(**)
- P7 pad 1: SO5 -> /14(Tx3)
- P7 pad 2: SO6 -> /15(Rx3)
- P7 pad 5: KitchenTTL -> /18(Tx1)
- P7 pad 6: BathRoomTTL -> /19(Rx1)
- P7 pad 7: SDA -> /20(SDA)
- P7 pad 8: SCL -> /21(SCL)
- Q10 pad 1: GND -> /34
- Q10 pad 2: GreyV -> Net-(Q10-Pad2)
- Q10 pad 3: Net-(Q10-Pad3) -> +5V
- Q11 pad 1: Net-(Q11-Pad1) -> /23
- Q11 pad 2: IO110 -> Net-(I1-Pad1)
- Q11 pad 3: Net-(Q11-Pad3) -> +5V
- Q12 pad 1: G1-4 -> /2(**)
- Q12 pad 2: IO13 -> Net-(I1-Pad2)
- Q13 pad 1: G1-2 -> /3(**)
- Q13 pad 2: IO16 -> Net-(I1-Pad3)
- Q14 pad 1: G4-4 -> /25
- Q14 pad 2: IO112 -> Net-(I1-Pad4)
- Q15 pad 1: G3-4 -> /29
- Q15 pad 2: IO19 -> Net-(O1-Pad1)
- Q15 pad 3: +5V -> GND
- Q16 pad 1: AlarmTTL -> /39
- Q16 pad 2: IO212 -> Net-(I1-Pad5)
- Q17 pad 1: KitchenTTL -> /31
- Q17 pad 2: IO29 -> Net-(O1-Pad2)
- Q17 pad 3: +5V -> GND
- Q18 pad 1: SpareTTL -> /18(Tx1)
- Q18 pad 2: IO23 -> Net-(I1-Pad6)
- Q19 pad 1: BathRoomTTL -> /33
- Q19 pad 2: IO26 -> Net-(O1-Pad3)
- Q19 pad 3: +5V -> GND
- Q2 pad 1: GND -> /48
- Q2 pad 2: STV -> Net-(Q2-Pad2)
- Q2 pad 3: Net-(Q2-Pad3) -> +5V
- Q20 pad 1: WPS -> /19(Rx1)
- Q20 pad 2: IO24 -> Net-(I1-Pad12)
- Q21 pad 1: ENLCD -> /35
- Q21 pad 2: IO412 -> Net-(O1-Pad4)
- Q21 pad 3: +5V -> GND
- Q22 pad 1: LCBBACK -> Net-(K4-Pad6)
- Q22 pad 2: IO27 -> Net-(Q22-Pad2)
- Q22 pad 3: +5V -> GND
- Q23 pad 1: WSS -> /28
- Q23 pad 2: IO311 -> Net-(I1-Pad11)
- Q24 pad 1: SPIn1 -> /37
- Q24 pad 2: IO41 -> Net-(O1-Pad5)
- Q24 pad 3: +5V -> GND
- Q25 pad 1: SPIn3 -> /27
- Q25 pad 2: IO47 -> Net-(I1-Pad10)
- Q26 pad 1: SPIn5 -> /12(**)
- Q26 pad 2: IO31 -> Net-(I1-Pad9)
- Q27 pad 1: SPIn6 -> /9(**)
- Q27 pad 2: IO34 -> Net-(O1-Pad6)
- Q27 pad 3: +5V -> GND
- Q28 pad 1: SPIn2 -> /11(**)
- Q28 pad 2: IO44 -> Net-(I1-Pad8)
- Q29 pad 1: SPIn4 -> /26
- Q29 pad 2: IO410 -> Net-(O1-Pad12)
- Q29 pad 3: +5V -> GND
- Q3 pad 1: Net-(Q3-Pad1) -> /46
- Q3 pad 2: IO17 -> Net-(Q3-Pad2)
- Q3 pad 3: Net-(Q3-Pad3) -> +5V
- Q30 pad 1: GND -> /10(**)
- Q30 pad 2: WSiren -> Net-(I1-Pad7)
- Q30 pad 3: Net-(Q30-Pad3) -> +5V
- Q31 pad 1: GND -> /8(**)
- Q31 pad 2: BRLED -> Net-(O1-Pad10)
- Q31 pad 3: Net-(Q31-Pad3) -> GND
- Q32 pad 1: Net-(Q32-Pad1) -> Net-(O1-Pad11)
- Q32 pad 2: IO211 -> Net-(Q32-Pad2)
- Q32 pad 3: +12V -> GND
- Q33 pad 1: Net-(Q33-Pad1) -> /24
- Q33 pad 2: IO25 -> Net-(IO1-Pad9)
- Q33 pad 3: +12V -> +5V
- Q36 pad 1: GND -> /7(**)
- Q36 pad 2: WLED -> Net-(O1-Pad9)
- Q36 pad 3: Net-(Q36-Pad3) -> GND
- Q37 pad 1: Net-(Q37-Pad1) -> /D22
- Q37 pad 2: IO22 -> Net-(IO1-Pad8)
- Q37 pad 3: +12V -> +5V
- Q38 pad 1: GND -> /6(**)
- Q38 pad 2: WP -> Net-(O1-Pad8)
- Q38 pad 3: Net-(Q38-Pad3) -> GND
- Q39 pad 1: Net-(Q39-Pad1) -> /5(**)
- Q39 pad 2: IO35 -> Net-(O1-Pad7)
- Q39 pad 3: +12V -> GND
- Q4 pad 1: S1-4 -> /44
- Q4 pad 2: IO12 -> Net-(Q4-Pad2)
- Q5 pad 1: S1-2 -> /42
- Q5 pad 2: IO15 -> Net-(Q5-Pad2)
- Q6 pad 1: S4-4 -> Net-(K2-Pad6)
- Q6 pad 2: IO111 -> Net-(Q6-Pad2)
- Q6 pad 3: +5V -> GND
- Q7 pad 1: S3-4 -> /40
- Q7 pad 2: IO18 -> Net-(Q7-Pad2)
- Q8 pad 1: GND -> /38
- Q8 pad 2: RTankPOWER -> Net-(Q8-Pad2)
- Q8 pad 3: Net-(Q8-Pad3) -> +5V
- Q9 pad 1: Net-(Q9-Pad1) -> /36
- Q9 pad 2: IO14 -> Net-(Q9-Pad2)
- Q9 pad 3: Net-(LPWater1-Pad1) -> +5V
- R11 pad 1: GND -> Net-(Q3-Pad2)
- R11 pad 2: A15 -> GND
- R12 pad 1: GND -> /46
- R12 pad 2: A12 -> GND
- R13 pad 1: GND -> Net-(Q4-Pad2)
- R13 pad 2: A13 -> GND
- R14 pad 1: GND -> /44
- R14 pad 2: Net-(D3-Pad1) -> GND
- R15 pad 1: STV -> Net-(Q5-Pad2)
- R16 pad 1: Net-(Q3-Pad3) -> GND
- R16 pad 2: Net-(Q3-Pad1) -> /A3
- R17 pad 1: Net-(Q3-Pad1) -> GND
- R17 pad 2: Net-(Q2-Pad3) -> /A4
- R18 pad 1: IO12 -> /42
- R19 pad 1: IO15 -> GND
- R19 pad 2: GND -> /A5
- R20 pad 1: S1-4 -> GND
- R20 pad 2: GND -> /A6
- R21 pad 1: S1-2 -> GND
- R21 pad 2: GND -> /A7
- R22 pad 1: IO111 -> GND
- R22 pad 2: GND -> /A9
- R23 pad 1: IO18 -> GND
- R23 pad 2: GND -> /A10
- R24 pad 1: S4-4 -> GND
- R24 pad 2: GND -> /A8
- R26 pad 1: GND -> Net-(Q6-Pad2)
- R26 pad 2: A11 -> /32
- R27 pad 2: A3 -> Net-(Q6-Pad2)
- R31 pad 1: GND -> Net-(Q7-Pad2)
- R31 pad 2: A8 -> GND
- R32 pad 1: GND -> /40
- R32 pad 2: A7 -> GND
- R33 pad 1: GND -> Net-(Q8-Pad2)
- R33 pad 2: A6 -> GND
- R34 pad 1: GND -> /38
- R34 pad 2: A5 -> GND
- R35 pad 2: A0 -> /A0
- R37 pad 1: Net-(Q9-Pad1) -> Net-(Q9-Pad2)
- R37 pad 2: Net-(Q8-Pad3) -> GND
- R38 pad 1: A1 -> /36
- R38 pad 2: IO14 -> GND
- R39 pad 1: GND -> Net-(Q10-Pad2)
- R39 pad 2: A2 -> GND
- R40 pad 1: GreyV -> /34
- R41 pad 1: Net-(Q11-Pad3) -> Net-(I1-Pad1)
- R41 pad 2: Net-(Q11-Pad1) -> GND
- R42 pad 1: Net-(Q11-Pad1) -> /23
- R42 pad 2: Net-(Q10-Pad3) -> GND
- R43 pad 1: IO13 -> Net-(I1-Pad2)
- R44 pad 1: IO16 -> /2(**)
- R45 pad 1: G1-4 -> Net-(I1-Pad3)
- R46 pad 1: G1-2 -> /3(**)
- R47 pad 1: IO112 -> Net-(I1-Pad4)
- R48 pad 1: IO19 -> /25
- R49 pad 1: G4-4 -> /29
- R5 pad 2: SCL -> /21(SCL)
- R50 pad 1: G3-4 -> Net-(I1-Pad5)
- R51 pad 1: IO212 -> /39
- R52 pad 1: IO29 -> /31
- R53 pad 1: AlarmTTL -> Net-(I1-Pad6)
- R54 pad 1: KitchenTTL -> /18(Tx1)
- R55 pad 1: IO23 -> Net-(I1-Pad12)
- R56 pad 1: IO26 -> /33
- R57 pad 1: SpareTTL -> /19(Rx1)
- R58 pad 1: BathRoomTTL -> Net-(Q22-Pad2)
- R58 pad 2: GND -> /43
- R59 pad 1: IO24 -> Net-(I1-Pad11)
- R6 pad 2: SDA -> /20(SDA)
- R60 pad 1: IO412 -> /35
- R61 pad 1: IO27 -> GND
- R61 pad 2: GND -> Net-(Q22-Pad2)
- R62 pad 1: IO311 -> /28
- R63 pad 1: WPS -> Net-(I1-Pad10)
- R64 pad 1: ENLCD -> /37
- R65 pad 1: LCBBACK -> /27
- R66 pad 1: WSS -> Net-(I1-Pad9)
- R67 pad 1: IO41 -> /9(**)
- R68 pad 1: IO47 -> /12(**)
- R69 pad 1: IO31 -> Net-(I1-Pad8)
- R70 pad 1: SPIn1 -> GND
- R70 pad 2: GND -> /A1
- R71 pad 1: SPIn3 -> /26
- R72 pad 1: SPIn5 -> /11(**)
- R73 pad 1: IO34 -> Net-(I1-Pad7)
- R74 pad 1: IO44 -> GND
- R74 pad 2: GND -> /A2
- R75 pad 1: IO410 -> /10(**)
- R76 pad 1: SPIn6 -> Net-(Q32-Pad2)
- R76 pad 2: GND -> /4(**)
- R77 pad 1: SPIn2 -> /8(**)
- R78 pad 1: SPIn4 -> GND
- R78 pad 2: GND -> Net-(Q32-Pad2)
- R79 pad 1: WSiren -> Net-(IO1-Pad9)
- R80 pad 1: BRLED -> /24
- R84 pad 1: Net-(Q33-Pad1) -> /7(**)
- R84 pad 2: Net-(Q31-Pad3) -> GND
- R85 pad 1: KLED -> Net-(IO1-Pad8)
- R86 pad 1: +12V -> /D22
- R86 pad 2: Net-(Q35-Pad1) -> GND
- R87 pad 1: Net-(Q35-Pad1) -> /6(**)
- R87 pad 2: Net-(Q34-Pad3) -> GND
- R88 pad 1: WLED -> /5(**)
- RTCBattery1 pad 1: A14 -> Net-(IC3-Pad14)
- Tanks1 pad 1: Net-(Q3-Pad3) -> Net-(K1-Pad7)
- Tanks2 pad 1: A2 -> Net-(Q2-Pad2)
- Tanks2 pad 10: IO110 -> Net-(K2-Pad1)
- Tanks2 pad 11: IO111 -> /A14
- Tanks2 pad 12: IO112 -> /A15
- Tanks2 pad 2: IO12 -> Net-(Q3-Pad2)
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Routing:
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- added copper zone on F.Cu, net GND
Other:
- board text added: "Holding Tank Sensors"
- board text added: "OUTPUTS"
- board text added: "RS232"
- board text added: "SDA SCL GND 5V"
- board text added: "Version: 0.6"
- board text added: "Voltage Sensor"
- board text removed: "Version: 1.0 ALPHA"
